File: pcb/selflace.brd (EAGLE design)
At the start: 24.1 x 47 mm, 49 parts, among them IC1 78L05Z, J3 AVR_SPI_PROG_3X2NS, U1 ATMEGA328P_TQFP, Y1 16MHz

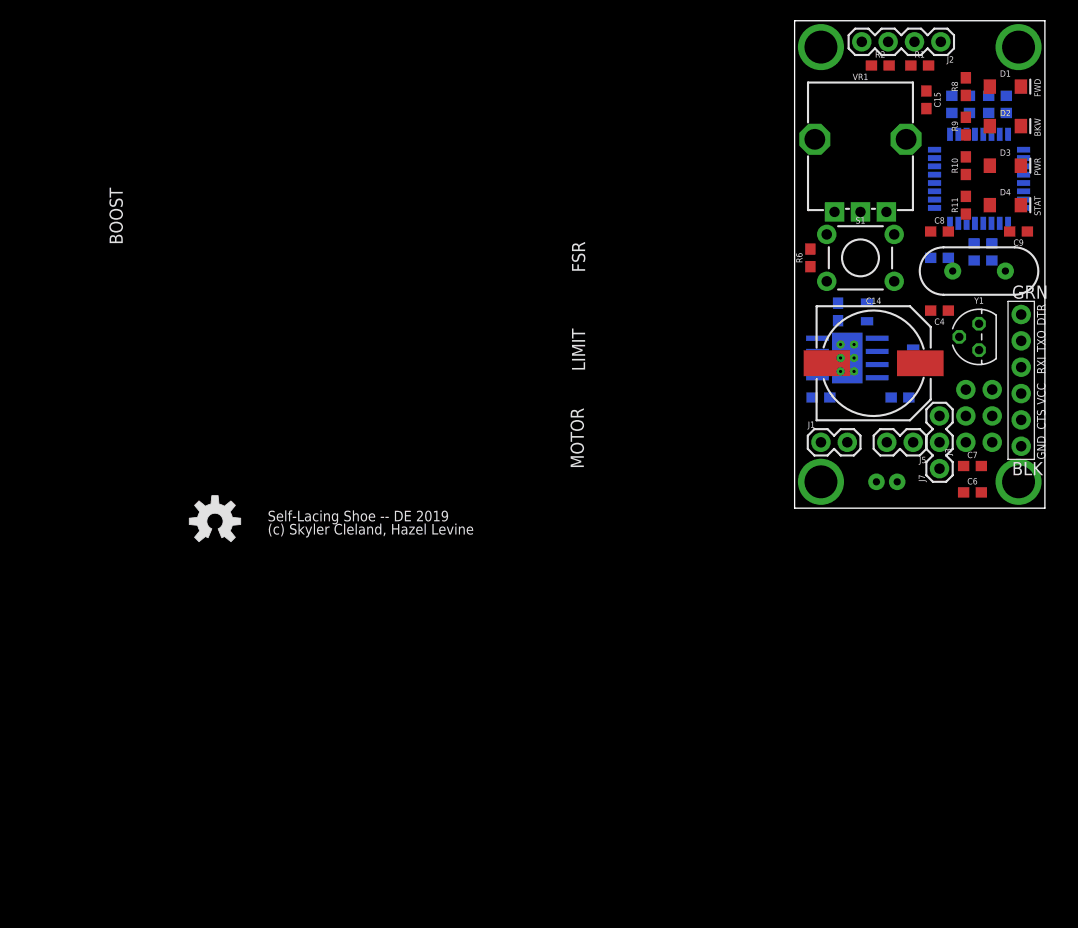
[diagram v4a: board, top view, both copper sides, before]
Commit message: update board to size specs and increase power/ground trace width
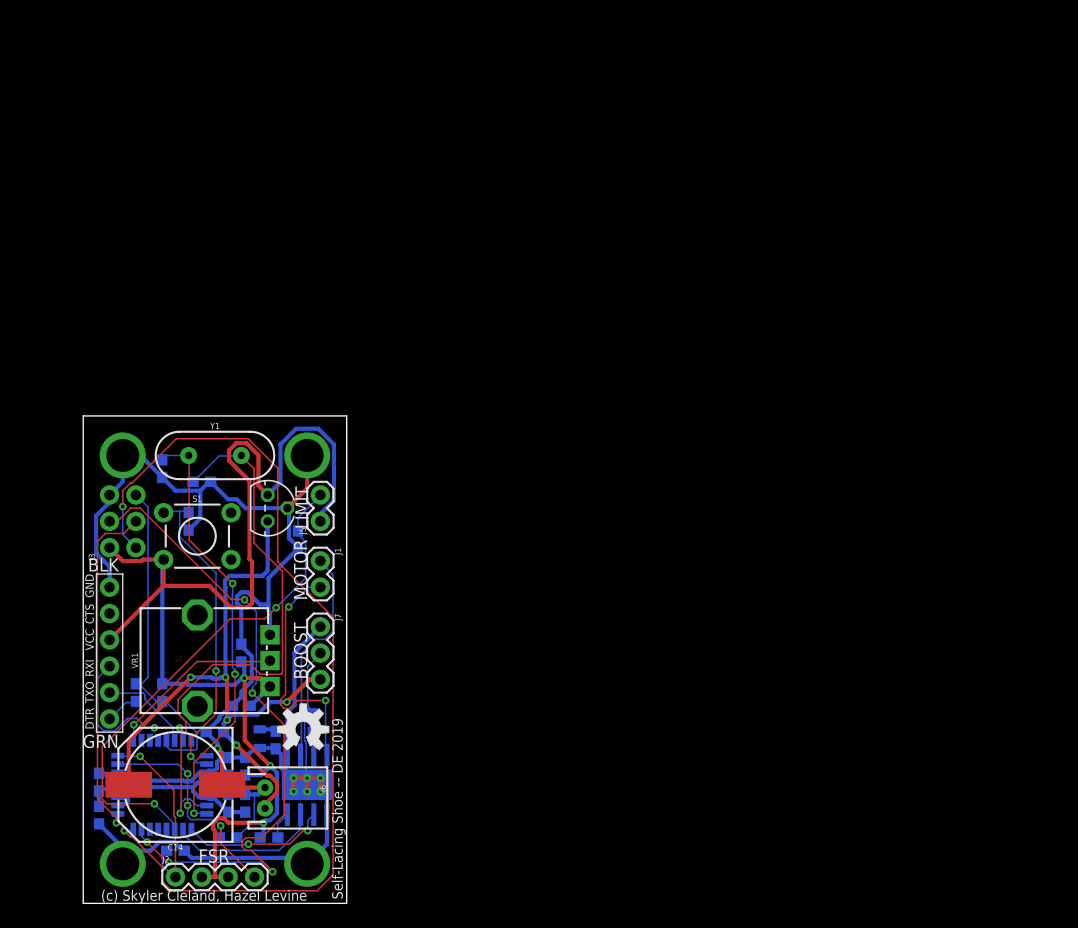
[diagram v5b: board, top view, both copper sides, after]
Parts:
- removed D1: FWD, SparkFun-LED:LED-1206
- removed D2: BKWD, SparkFun-LED:LED-1206
- removed D3: POWER, SparkFun-LED:LED-1206
- removed D4: STATE, SparkFun-LED:LED-1206
- removed FRAME1: FRAME-LEDGER, SparkFun-Aesthetics:CREATIVE_COMMONS
- removed R10, R11, R8, R9: 220, SparkFun-Resistors:0603
- moved J2 109.2 mm to (8.89, 2.54), turned to 0 degrees
- moved R1 104.3 mm to (8.89, 5.08), flipped to the bottom
- moved C5 100.6 mm to (1.52, 8.51), turned to 270 degrees
- moved C1 99.8 mm to (1.52, 11.7), turned to 90 degrees
- moved C11 99.6 mm to (14.0, 9.65), turned to 90 degrees
- moved C10 99.5 mm to (15.6, 9.65), turned to 90 degrees
- moved U1 98.0 mm to (7.62, 11.4), turned to 0 degrees
- moved R2 97.4 mm to (14.0, 6.35), flipped to the bottom
- moved C13 94.6 mm to (14.0, 13.2), turned to 90 degrees
- moved C12 94.5 mm to (15.6, 13.2), turned to 90 degrees
- moved J4 91.7 mm to (2.54, 24.1), turned to 90 degrees
- moved R5 85.9 mm to (7.62, 20.3), turned to 90 degrees
- moved C4 85.8 mm to (5.08, 20.3), flipped to the bottom, turned to 90 degrees
- moved C9 85.7 mm to (7.62, 41.9), flipped to the bottom, turned to 270 degrees
- moved C15 84.9 mm to (15.2, 24.1), flipped to the bottom, turned to 90 degrees
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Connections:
- removed net N$13: D1.A, R8.2
- removed net N$14: D2.A, R9.2
- removed net N$15: D3.A, R10.2
- removed net N$16: D4.A, R11.2
- net DIG2: no longer R8.1
- net DIG3: no longer R9.1
- net DIG8: no longer R10.1
- net DIG9: no longer R11.1
- net GND: no longer D1.C, D2.C, D3.C, D4.C
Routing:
- net GND: track 0.00 -> 174.2 mm, vias 0 -> 1
- net VCC: track 0.00 -> 154.6 mm, vias 0 -> 3
- net MISO: track 0.00 -> 90.5 mm, vias 0 -> 2
- net MOSI: track 0.00 -> 64.1 mm, vias 0 -> 5
- net N$12: track 0.00 -> 61.3 mm, vias 0 -> 5
- net N$7: track 0.00 -> 55.6 mm, vias 0 -> 1
- net N$2: track 0.00 -> 49.1 mm, vias 0 -> 2
- net N$11: track 0.00 -> 42.0 mm, vias 0 -> 3
- net SCK: track 0.00 -> 33.3 mm, vias 0 -> 1
- net RESET: track 0.00 -> 32.7 mm
- net N$1: track 0.00 -> 30.6 mm, vias 0 -> 2
- net N$5: track 0.00 -> 23.9 mm, vias 0 -> 2
- net N$9: track 0.00 -> 22.3 mm, vias 0 -> 3
- net N$4: track 0.00 -> 21.0 mm
- net N$10: track 0.00 -> 18.6 mm, vias 0 -> 1
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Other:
- board size 24.1 x 47 mm -> 25.4 x 47 mm
- board text removed: "BKW"
- board text removed: "FWD"
- board text removed: "PWR"
- board text removed: "STAT"

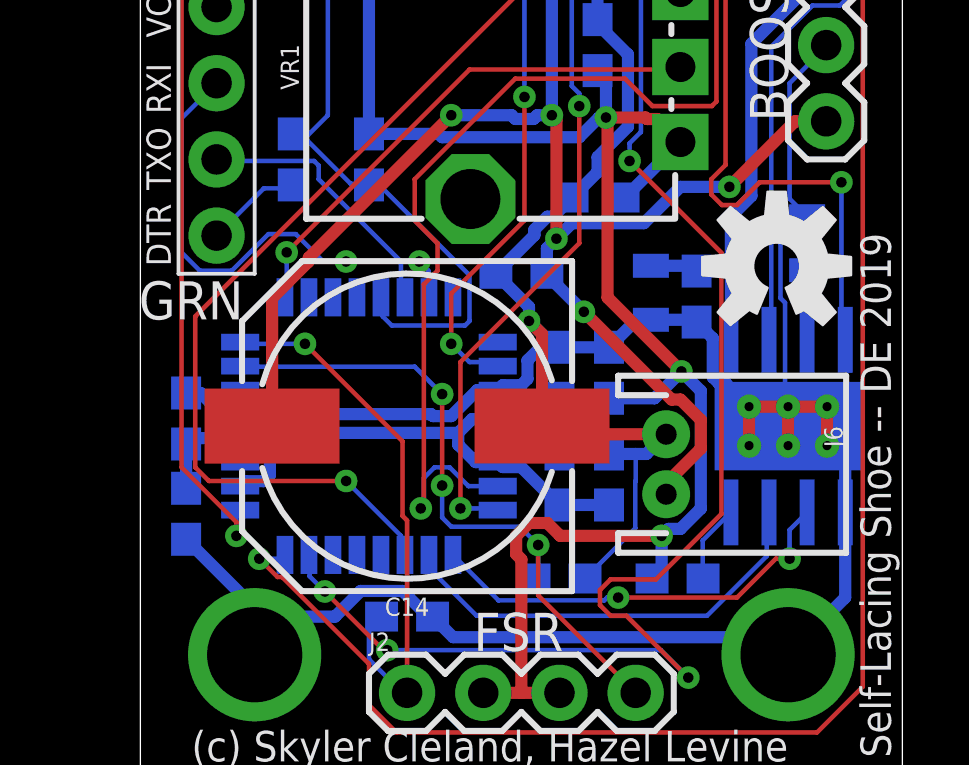
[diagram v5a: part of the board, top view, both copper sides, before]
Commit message: add sch border back, fix wire stubs
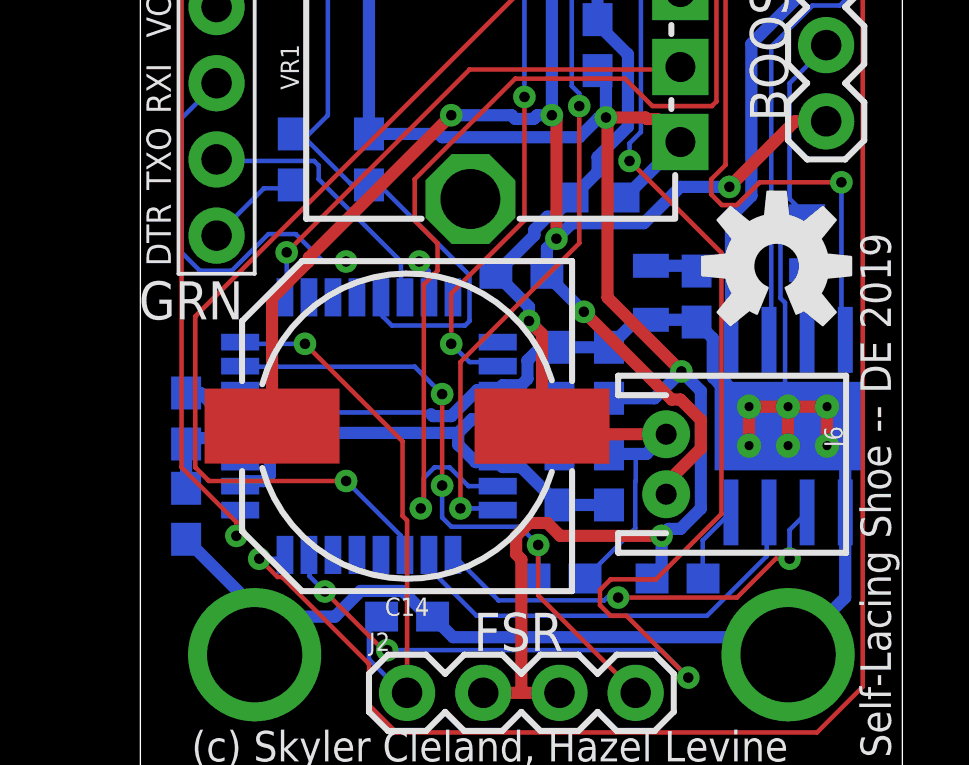
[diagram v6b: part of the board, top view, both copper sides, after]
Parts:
- added FRAME1: FRAME-LEDGER, SparkFun-Aesthetics:CREATIVE_COMMONS
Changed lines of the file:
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@@
 <attribute name="VALUE" x="14.478" y="24.13" size="0.6096" layer="28" font="vector" ratio="20" rot="MR90" align="top-center"/>
 </element>
+<element name="FRAME1" library="SparkFun-Aesthetics" library_urn="urn:adsk.eagle:library:507" package="CREATIVE_COMMONS" package3d_urn="urn:adsk.eagle:package:37121/1" value="FRAME-LEDGER" x="20.828" y="-7.874" smashed="yes"/>
 </elements>
 <signals>
@@
 <contactref element="U1" pad="20"/>
 <contactref element="C15" pad="1"/>
-<wire x1="17.1958" y1="6.4008" x2="17.057" y2="6.35" width="0.1524" layer="16"/>
-<wire x1="12.0396" y1="11.8872" x2="11.9126" y2="11.83" width="0.1524" layer="16"/>
-<wire x1="11.8872" y1="11.7348" x2="11.9126" y2="11.83" width="0.1524" layer="16"/>
 <wire x1="16.1544" y1="19.05" x2="16.09" y2="19.05" width="0.1524" layer="16"/>
 <via x="15.5194" y="21.717" extent="1-16" drill="0.35"/>
@@
 <wire x1="17.6056" y1="8.0044" x2="18.00466875" y2="8.0044" width="0.4064" layer="16"/>
 <wire x1="17.3736" y1="7.7724" x2="17.6056" y2="8.0044" width="0.4064" layer="16"/>
-<wire x1="17.057" y1="6.35" x2="17.3736" y2="6.6666" width="0.4064" layer="16"/>
 <wire x1="17.3736" y1="6.6666" x2="17.3736" y2="7.7724" width="0.4064" layer="16"/>
-<wire x1="1.524" y1="10.834" x2="1.7454" y2="10.834" width="0.4064" layer="16"/>
 <wire x1="4.10969375" y1="10.865" x2="4.318" y2="10.65669375" width="0.4064" layer="16"/>
 <wire x1="4.318" y1="10.65669375" x2="4.318" y2="9.80330625" width="0.4064" layer="16"/>
@@
 <wire x1="15.28715" y1="21.717" x2="15.5194" y2="21.717" width="0.4064" layer="16"/>
 <wire x1="14.62955" y1="21.0594" x2="15.28715" y2="21.717" width="0.4064" layer="16"/>
-<wire x1="1.524" y1="10.834" x2="1.72" y2="11.03" width="0.4064" layer="16"/>
 <wire x1="1.72" y1="11.03" x2="3.3274" y2="11.03" width="0.4064" layer="16"/>
 <wire x1="1.524" y1="9.359" x2="1.524" y2="10.834" width="0.4064" layer="16"/>
@@
 <wire x1="17.78" y1="39.37" x2="19.0119" y2="40.6019" width="0.4064" layer="16"/>
 <wire x1="19.0119" y1="40.6019" x2="19.0119" y2="44.2478875" width="0.4064" layer="16"/>
+<wire x1="17.2212" y1="6.5532" x2="17.0688" y2="6.4008" width="0.1524" layer="16"/>
+<wire x1="17.0688" y1="6.4008" x2="17.057" y2="6.35" width="0.1524" layer="16"/>
+<wire x1="17.2212" y1="6.5532" x2="17.3736" y2="6.6666" width="0.1524" layer="16"/>
+<wire x1="12.0396" y1="11.8872" x2="11.9126" y2="11.83" width="0.1524" layer="16"/>
+<wire x1="1.524" y1="10.9728" x2="1.524" y2="10.834" width="0.1524" layer="16"/>
+<wire x1="1.524" y1="10.9728" x2="1.72" y2="11.03" width="0.1524" layer="16"/>
 </signal>
 <signal name="GND">
@@
 <contactref element="MGT3" pad="P$1"/>
 <contactref element="C15" pad="2"/>
-<wire x1="14.0208" y1="10.5156" x2="13.97" y2="10.502" width="0.1524" layer="16"/>
-<wire x1="3.2004" y1="11.8872" x2="3.3274" y2="11.83" width="0.1524" layer="16"/>
 <wire x1="22.86" y1="24.0792" x2="21.6408" y2="22.86" width="0.1524" layer="16"/>
 <wire x1="22.86" y1="24.13" x2="22.86" y2="24.0792" width="0.1524" layer="16"/>
@@
 <wire x1="23.495" y1="10.175" x2="22.89" y2="10.78" width="0.4064" layer="16"/>
 <wire x1="2.54510625" y1="11.995" x2="3.1624" y2="11.995" width="0.4064" layer="16"/>
-<wire x1="3.1624" y1="11.995" x2="3.3274" y2="11.83" width="0.4064" layer="16"/>
 <wire x1="1.524" y1="12.534" x2="2.00610625" y2="12.534" width="0.4064" layer="16"/>
 <wire x1="2.00610625" y1="12.534" x2="2.54510625" y2="11.995" width="0.4064" layer="16"/>
@@
 <wire x1="11.22935" y1="12.63" x2="11.9126" y2="12.63" width="0.4064" layer="16"/>
 <wire x1="10.36235" y1="11.763" x2="11.22935" y2="12.63" width="0.4064" layer="16"/>
-<wire x1="3.3274" y1="11.83" x2="9.68745" y2="11.83" width="0.4064" layer="16"/>
 <wire x1="9.68745" y1="11.83" x2="9.75445" y2="11.763" width="0.4064" layer="16"/>
 <wire x1="13.3406" y1="14.058" x2="13.8312" y2="14.058" width="0.4064" layer="16"/>
@@
 <wire x1="11.9126" y1="11.03" x2="13.442" y2="11.03" width="0.4064" layer="16"/>
 <wire x1="13.442" y1="11.03" x2="13.97" y2="10.502" width="0.4064" layer="16"/>
-<wire x1="15.621" y1="10.502" x2="13.97" y2="10.502" width="0.4064" layer="16"/>
 <wire x1="2.54" y1="39.37" x2="2.54" y2="38.661975" width="0.4064" layer="16"/>
 <wire x1="2.54" y1="32.458025" x2="2.54" y2="30.48" width="0.4064" layer="16"/>
@@
 <wire x1="14.82" y1="6.35" x2="16.4974" y2="8.0274" width="0.1524" layer="16"/>
 <wire x1="16.4974" y1="8.0274" x2="16.4974" y2="9.5860625" width="0.1524" layer="16"/>
+<wire x1="3.2004" y1="11.8872" x2="3.3274" y2="11.83" width="0.1524" layer="16"/>
+<wire x1="3.2004" y1="11.8872" x2="3.1624" y2="11.995" width="0.1524" layer="16"/>
+<wire x1="9.6012" y1="11.8872" x2="3.3528" y2="11.8872" width="0.1524" layer="16"/>
+<wire x1="3.3528" y1="11.8872" x2="3.3274" y2="11.83" width="0.1524" layer="16"/>
+<wire x1="9.6012" y1="11.8872" x2="9.75445" y2="11.763" width="0.1524" layer="16"/>
+<wire x1="15.5448" y1="10.5156" x2="14.0208" y2="10.5156" width="0.1524" layer="16"/>
+<wire x1="14.0208" y1="10.5156" x2="13.97" y2="10.502" width="0.1524" layer="16"/>
+<wire x1="15.5448" y1="10.5156" x2="15.621" y2="10.502" width="0.1524" layer="16"/>
 </signal>
 <signal name="N$4">
@@
 <contactref element="U2" pad="P$8"/>
 <contactref element="J1" pad="2"/>
-<wire x1="23.241" y1="19.431" x2="23.368" y2="19.558" width="0.1524" layer="1"/>
 <via x="23.368" y="19.558" extent="1-16" drill="0.35"/>
 <wire x1="23.368" y1="19.558" x2="23.368" y2="14.432" width="0.1524" layer="16"/>
@@
 <contactref element="J7" pad="1"/>
 <wire x1="18.4912" y1="16.6624" x2="18.542" y2="16.598" width="0.1524" layer="16"/>
-<wire x1="19.5326" y1="14.4286" x2="19.685" y2="14.305" width="0.1524" layer="16"/>
-<wire x1="18.4912" y1="16.6624" x2="18.3786" y2="16.775" width="0.1524" layer="16"/>
 <wire x1="19.685" y1="18.41865" x2="19.685" y2="16.51" width="0.4064" layer="16"/>
 <wire x1="19.685" y1="16.51" x2="19.685" y2="14.305" width="0.4064" layer="16"/>
@@
 <wire x1="16.4592" y1="41.91" x2="16.4592" y2="34.7472" width="0.1524" layer="1"/>
 <wire x1="15.24" y1="43.1292" x2="16.4592" y2="41.91" width="0.1524" layer="1"/>
-<wire x1="11.8872" y1="9.4488" x2="11.9126" y2="9.43" width="0.1524" layer="16"/>
 <wire x1="15.24" y1="43.18" x2="15.24" y2="43.1292" width="0.1524" layer="1"/>
 <via x="9.3472" y="8.6868" extent="1-16" drill="0.35"/>
@@
 <contactref element="C14" pad="+"/>
 <wire x1="13.5636" y1="16.4592" x2="13.55" y2="16.51" width="0.1524" layer="16"/>
-<wire x1="13.5636" y1="16.6116" x2="13.55" y2="16.51" width="0.1524" layer="16"/>
 <via x="14.7828" y="15.24" extent="1-16" drill="0.35"/>
 <via x="19.6342" y="19.4056" extent="1-16" drill="0.35"/>
@@
 <via x="13.8684" y="17.6784" extent="1-16" drill="0.35"/>
 <via x="13.716" y="21.7932" extent="1-16" drill="0.35"/>
-<wire x1="4.39" y1="11.43" x2="4.4196" y2="11.4596" width="0.1524" layer="1"/>
 <wire x1="18.6816" y1="10.68133125" x2="18.6816" y2="11.63866875" width="0.4064" layer="1"/>
 <wire x1="18.6816" y1="11.63866875" x2="18.00466875" y2="12.3156" width="0.4064" layer="1"/>
